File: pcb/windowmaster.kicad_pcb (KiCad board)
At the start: 2 copper layers, 100 x 50 mm, 73 parts, among them J1 USB_C_Receptacle_USB2.0, SW1 SW_DFU2, SW2 ENC1, SW3 ENC2, SW4 ENC3, SW5 ENC4, SW6 ENC5, SW7 ENC6, SW8 SW_DFU, SW9 SW_RST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

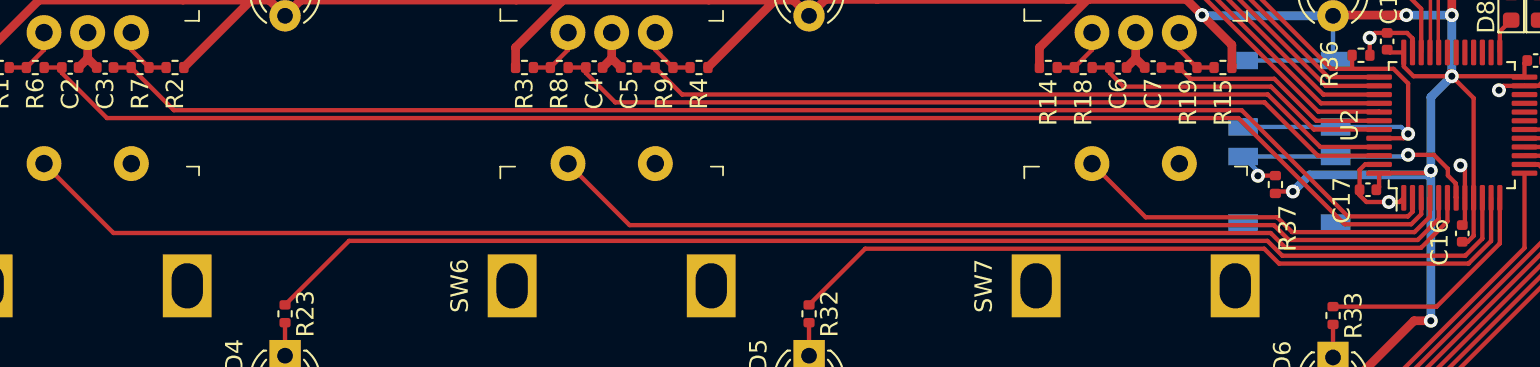
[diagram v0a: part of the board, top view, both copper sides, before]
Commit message: Rearrange vias to cut less into ground plane
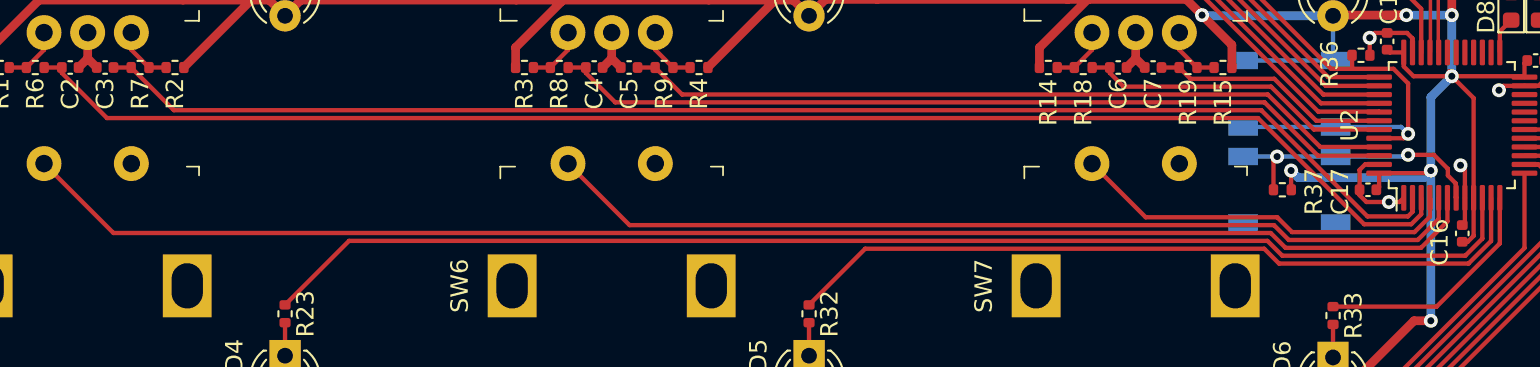
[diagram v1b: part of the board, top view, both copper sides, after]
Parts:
- moved R37 0.50 mm to (221.1, 110.5), turned to 180 degrees

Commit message: Separate the USB/MCU/power supply parts of the schematic
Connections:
- net /USB_D+ renamed USB_DP
- net /USB_D- renamed USB_DM
- net /USB_VBUS renamed VBUS

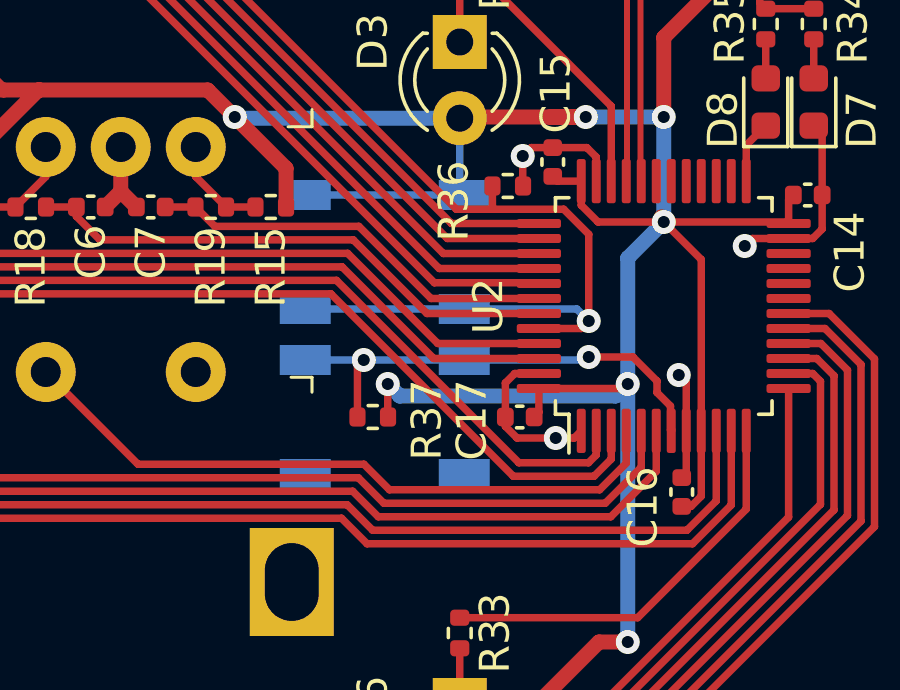
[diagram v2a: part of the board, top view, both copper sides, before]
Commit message: Add reset switch models to PCB and add case draft
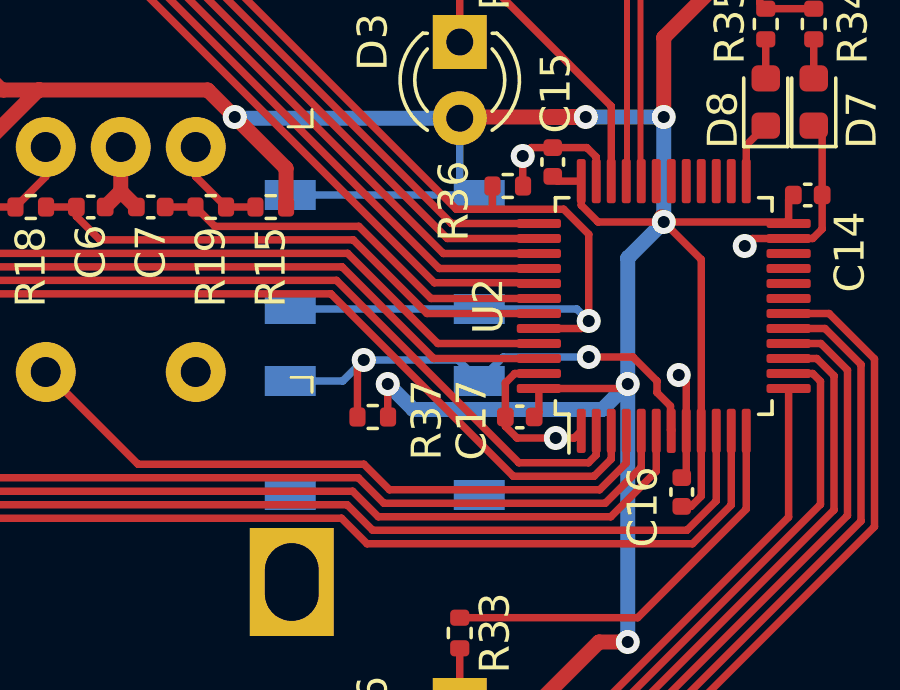
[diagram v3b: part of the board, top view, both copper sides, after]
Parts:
- SW8, SW9: footprint windowmaster:TL3342F160QG -> Button_Switch_SMD:SW_SPST_TL3342
- moved SW9 0.70 mm to (221.5, 111.2), turned to 180 degrees
- turned SW8 to 180 degrees
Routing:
- net NRST: track 16.0 -> 17.5 mm

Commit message: Add switch labels on PCB
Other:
- board text added: "Adam Gausmann 2021-02-21"
- board text added: "DFU"
- board text added: "RST"
- board text removed: "Adam Gausmann 2021-02-03"

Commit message: Hierarchical redesign and add ST-Link SWD header
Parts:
- added J2: SWD, Connector_PinHeader_2.54mm:PinHeader_1x06_P2.54mm_Vertical, F.Cu at (202.0, 83.1)
- D1: value LED1 -> LED
- D2: value LED2 -> LED
- D3: value LED3 -> LED
- D4: value LED4 -> LED
- D5: value LED5 -> LED
- D6: value LED6 -> LED
- J1: footprint windowmaster:TYPEC-304S-ACP16 -> windowmaster:HRO_TYPE-C-31-M-12
- SW2: value ENC1 -> ENC
- SW3: value ENC2 -> ENC
- SW4: value ENC3 -> ENC
- SW5: value ENC4 -> ENC
- SW6: value ENC5 -> ENC
- SW7: value ENC6 -> ENC
- moved SW1 2.70 mm to (195.3, 85.0)
- moved J1 1.84 mm to (225.2, 82.1)
- moved R10 1.20 mm to (226.7, 89.2)
- moved R11 1.20 mm to (223.7, 89.2)
- moved R22 0.86 mm to (224.5, 96.3), turned to 180 degrees
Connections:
- net USB_DM renamed USB_D-
- net USB_DP renamed USB_D+
- U2 pad 27: Net-(U2-Pad27) -> SW_3
- U2 pad 28: Net-(U2-Pad28) -> IND_3
- U2 pad 34: IND_3 -> SWDIO
- U2 pad 37: SW_3 -> SWCLK
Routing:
- net NRST: track 17.5 -> 61.2 mm, vias 2 -> 4
- net SWDIO: track 0.00 -> 32.8 mm
- net SWCLK: track 0.00 -> 31.8 mm
- net GND: track 68.4 -> 53.2 mm, vias 7 -> 6
- net SW_3: track 25.6 -> 31.3 mm, vias 0 -> 2
- net IND_3: track 9.64 -> 11.4 mm, vias 0 -> 2
- net VBUS: track 14.0 -> 12.8 mm
- net +3V3: track 328.3 -> 329.4 mm
- net DFU: track 54.6 -> 53.9 mm, vias 1 -> 3
- net USB_D-: track 21.1 -> 20.6 mm
- net USB_D+: track 20.1 -> 19.5 mm
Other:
- board text added: "Adam Gausmann 2021-03-10"
- board text added: "JLCJLCJLCJLC"
- board text added: "SWD"
- board text removed: "Adam Gausmann 2021-02-21"

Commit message: Final changes to PCB before ordering...
- Add external pull-ups to switch inputs.
- Double-check and fix LCSC part numbers.
- Add filter capacitor to regulator output.
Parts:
- added C18: 4.7uF, Capacitor_SMD:C_0402_1005Metric, F.Cu at (229.4, 90.7)
- added R38: 10K, Resistor_SMD:R_0402_1005Metric, F.Cu at (221.0, 93.1)
- added R39: 10K, Resistor_SMD:R_0402_1005Metric, F.Cu at (161.0, 112.0)
- added R40: 10K, Resistor_SMD:R_0402_1005Metric, F.Cu at (191.0, 89.5)
- added R41: 10K, Resistor_SMD:R_0402_1005Metric, F.Cu at (191.0, 111.5)
- added R42: 10K, Resistor_SMD:R_0402_1005Metric, F.Cu at (221.1, 111.6)
- added R5: 10K, Resistor_SMD:R_0402_1005Metric, F.Cu at (161.0, 90.0)
- C1: value 100nF -> 4.7uF
- R36, R37: value 5.1K -> 10K
- U2: value STM32F072C8Tx -> STM32F072C8T6
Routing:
- net +3V3: track 329.4 -> 461.9 mm, vias 9 -> 7
- net GND: track 53.2 -> 54.9 mm
- net SW_3: track 31.3 -> 32.1 mm
- net SW_5: track 53.4 -> 53.9 mm
- net SW_2: track 53.7 -> 54.2 mm
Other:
- board text added: "Adam Gausmann 2021-03-17"
- board text removed: "Adam Gausmann 2021-03-10"
